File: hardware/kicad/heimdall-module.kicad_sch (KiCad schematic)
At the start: 27 parts, among them J2 Breakout, U1 MC33269DT-3.3G, U2 ESP32-C3-WROOM-02-N4, U3 TYPEC-214-ARP14H105, U4 USBLC6-2SC6

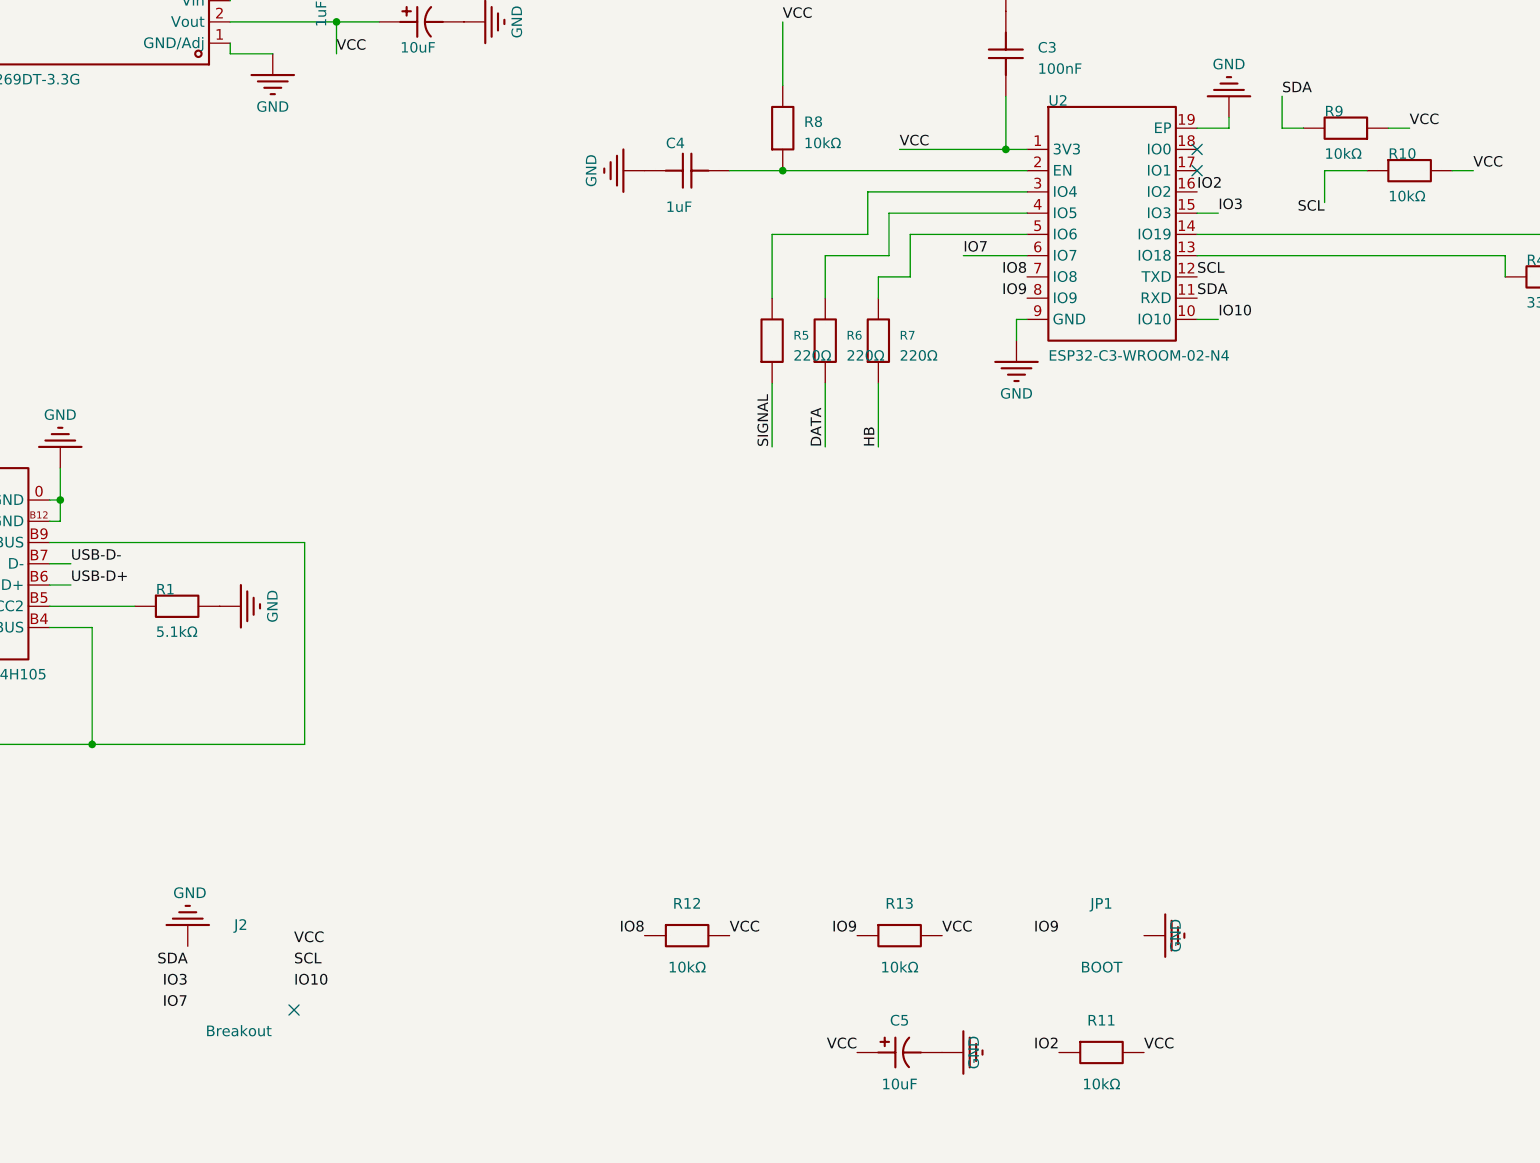
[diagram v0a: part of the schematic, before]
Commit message: Bay interface: Schottky isolation on all bay signal lines
The bay lines no longer connect straight to the ESP32 through 220R
(R5-R7 removed). Each line goes through a BAT54WS (D3-D6), the same
scheme as the DIY Multiprotocol module: the radio can only pull a line
low, and every high level comes from 3V3 pull-ups. A radio driving 5V
can't reach the ESP32.

- PPM in: D3 + R14 4.7k -> IO4
- DATA (CRSF, half duplex): RX D4 + R16 4.7k -> IO5, TX D5 <- IO6,
  R17 1.5k bay-side pull-up for fast rising edges
- HB out: D6 <- IO7, R15 4.7k bay-side pull-up
- Breakout J2 pin 7: IO7 -> IO1 (silk relabelled)

Board re-routed (prep -> Freerouting -> finish pipeline). DRC: 0 errors,
0 unconnected, 0 parity; only the known U3 A1 starved-thermal warning.

Co-Authored-By: Claude Opus 5.5 <noreply@anthropic.com>
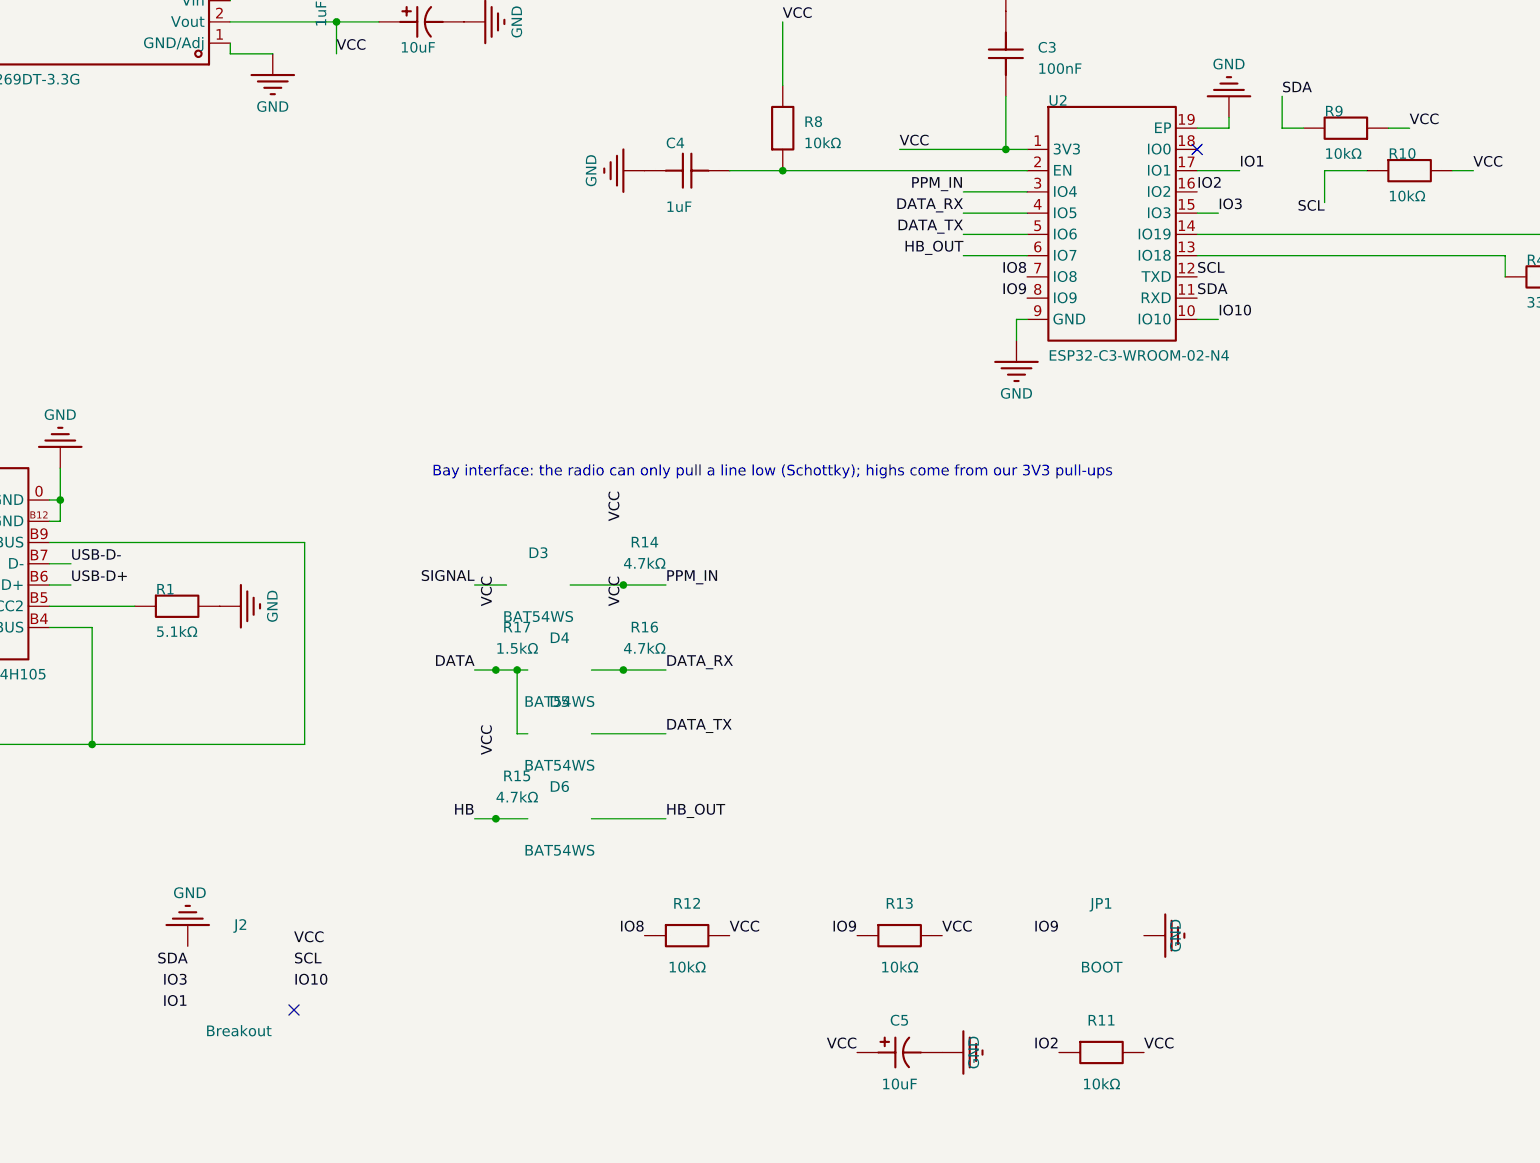
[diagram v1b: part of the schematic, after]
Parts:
- removed R5, R6, R7: 220Ω, heimdall-m-easyedapro:R0805, symbol heimdall-m-easyedapro:ERA6AEB221V
- added D3, D4, D5, D6: BAT54WS, Diode_SMD:D_SOD-323, symbol Device:D_Schottky
- added R14, R15, R16: 4.7kΩ, heimdall-m-easyedapro:R0805, symbol Device:R
- added R17: 1.5kΩ, heimdall-m-easyedapro:R0805, symbol Device:R
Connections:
- net DATA: now also D4.1 (K), D5.2 (A), R17.2
- net HB: now also D6.2 (A), R15.2
- net SIGNAL: now also D3.1 (K)
- net VCC: now also R14.1, R15.1, R16.1, R17.1
- net DATA_TX: now reaches U2.5 (IO6)
- net DATA_TX: now also D5.1 (K)
- net DATA_RX: now reaches U2.4 (IO5)
- net DATA_RX: now also D4.2 (A), R16.2
- net IO1: now reaches U2.17 (IO1)
- net IO1: now also J2.7 (Pin_7)
- net PPM_IN: now reaches U2.3 (IO4)
- net PPM_IN: now also D3.2 (A), R14.2
- net IO7 renamed HB_OUT
- net HB_OUT: now also D6.1 (K); no longer J2.7 (Pin_7)
- no-connect marks 3 -> 2
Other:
- note added: "Bay interface: the radio can only pull a line low (Schottky); highs come from our 3V3 pull-ups"

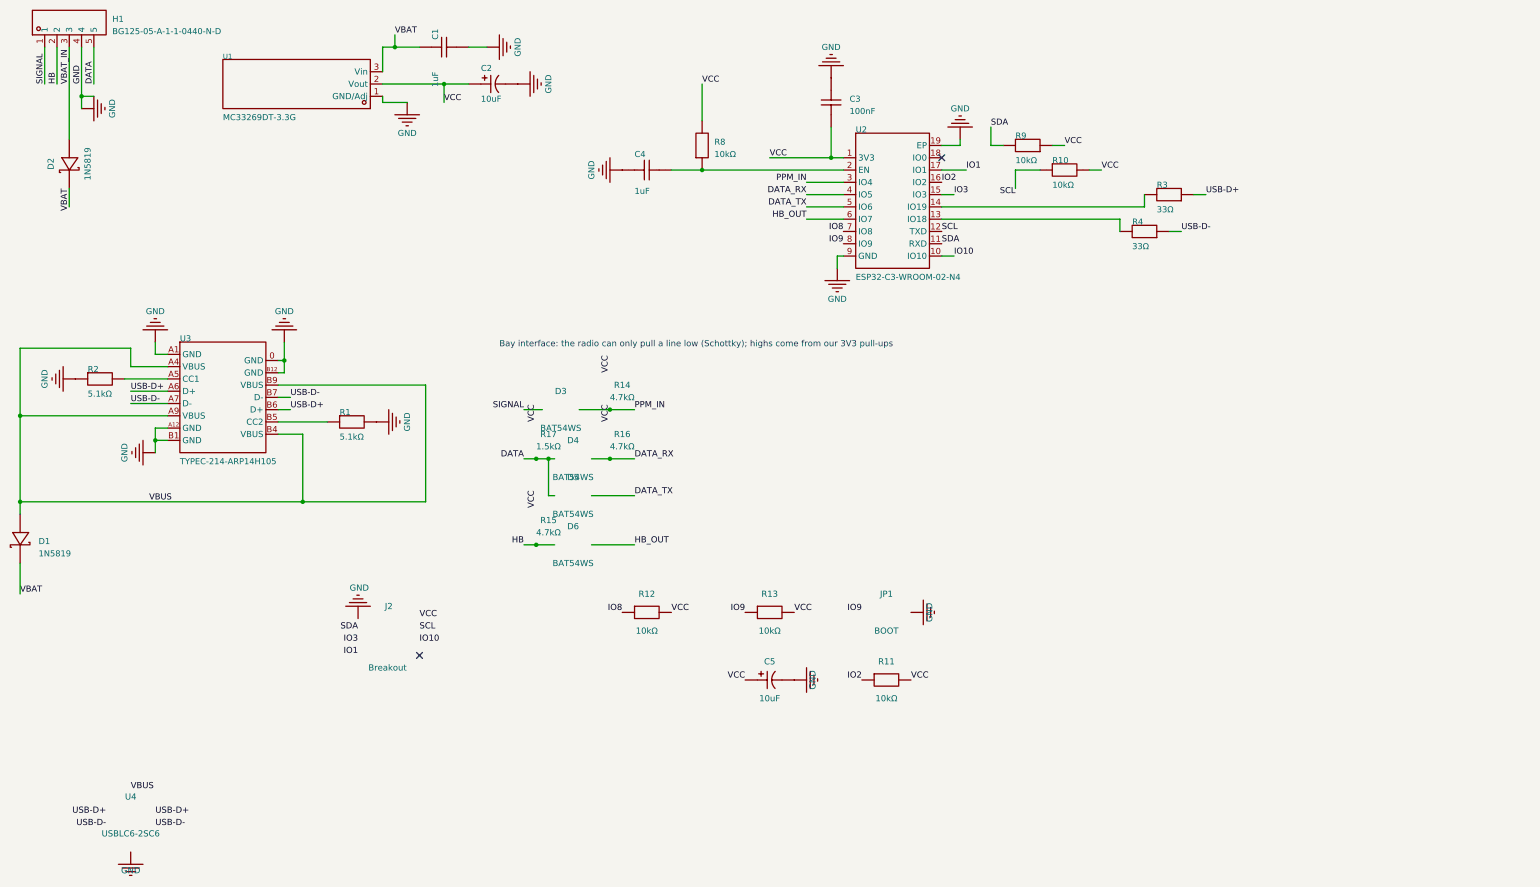
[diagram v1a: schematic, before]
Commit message: Bay DATA transmit through a 5V-tolerant buffer: S.Port and CRSF
The module has to talk S.Port (idle low, inverted) or CRSF (idle high)
on the DATA pin depending on what the internal module uses. The
pull-low-only diode and the 1.5k pull-up only worked for CRSF.

- D5 and the 1.5k pull-up out; U5 74LVC1G34 (always on) + R17 1k in.
  The UART idle level holds the line in either mode; the radio
  overrides 1k when it transmits.
- DATA_TX on IO7, HB_OUT on IO8 (R12 doubles as its pull-up), IO6 free.
- D6/R15 one step lower, R12/R13 0.3mm lower; DATA, HB, HB_OUT, D+/D-
  and the U5 supply hand-routed in route_pcb.py prep.

DRC: 0 unconnected, 0 parity. Two starved-thermal warnings: U3 A1 (as
before) and J2 pin 1 (plated through, connected on the bottom).

Co-Authored-By: Claude Opus 5.5 <noreply@anthropic.com>
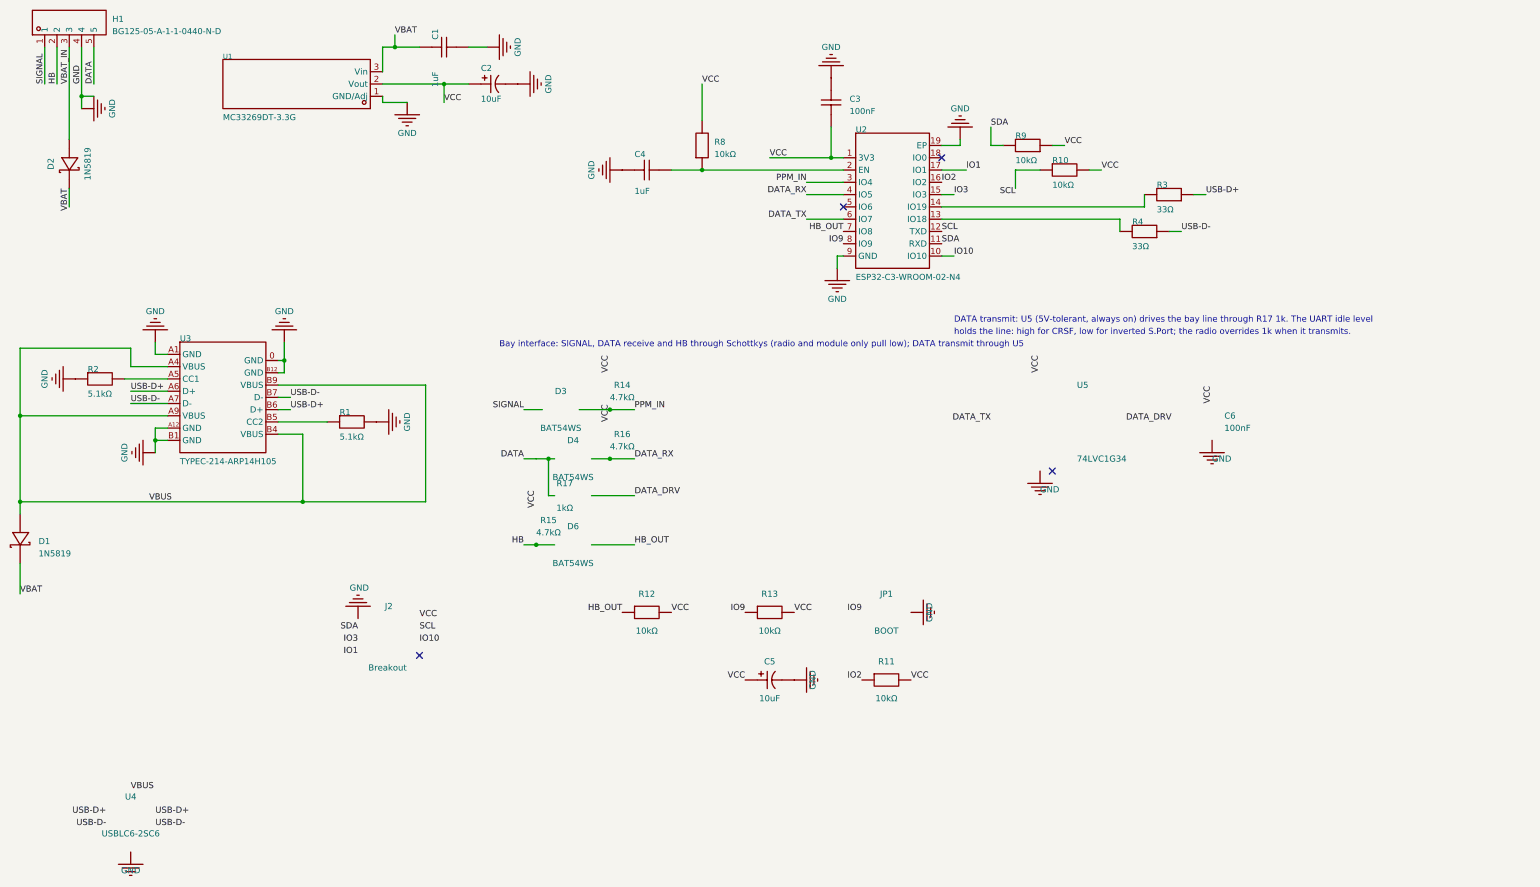
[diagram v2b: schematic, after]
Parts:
- removed D5: BAT54WS, Diode_SMD:D_SOD-323, symbol Device:D_Schottky
- added C6: 100nF, heimdall-m-easyedapro:C0805, symbol Device:C
- added U5: 74LVC1G34, Package_TO_SOT_SMD:SOT-23-5, symbol 74xGxx:74LVC1G34
- R17: value 1.5kΩ -> 1kΩ; Manufacturer Part ERJ-6ENF1501V -> ERJ-6ENF1001V
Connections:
- net IO8 is gone; now on net HB_OUT: R12.1, U2.7 (IO8)
- net DATA: now also R17.1; no longer R17.2
- net DATA_TX: now also U2.6 (IO7), U5.2; no longer U2.5 (IO6)
- net GND: now also C6.2, U5.3 (GND)
- net HB_OUT: no longer U2.6 (IO7)
- net VCC: now also C6.1, U5.5 (VCC); no longer R17.1
- new net DATA_DRV: R17.2, U5.4
- no-connect marks 2 -> 4
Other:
- note added: "Bay interface: SIGNAL, DATA receive and HB through Schottkys (radio and module only pull low); DATA transmit through U5"
- note added: "DATA transmit: U5 (5V-tolerant, always on) drives the bay line through R17 1k. The UART idle level"
- note added: "holds the line: high for CRSF, low for inverted S.Port; the radio overrides 1k when it transmits."
- note removed: "Bay interface: the radio can only pull a line low (Schottky); highs come from our 3V3 pull-ups"

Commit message: Fit the case's lid bosses, M2 screws, spread parts for hand soldering
Case fit (measured on the printed case):
- Board corners chamfered 45 deg (2.8mm legs): the lid screw bosses
  (1.7mm holes, 3.5mm bosses in the cavity corners) stopped the board
  on its way down to the standoffs. ~0.47mm left to each boss.
- MH1-MH3 3.2mm (M3) -> 2.2mm for 2mm self-tapping screws into the
  standoffs' 1.8mm pilots; the lid uses the same screws. Copper keepout
  stays 3mm.

Layout (spread_place.py, then the route_pcb.py flow re-run in full):
- Left of the module: >= 1mm between courtyards, parts in module pin
  order; HB and BOOT parts moved below the module, left of J1.
- U1 at the bottom edge with its heatsink copper; C1/C2 beside it.
- R3/R4 off the module and turned 180, D1 up from D2, R9/R10 apart.
- Hand routes for VCC, HB, SIGNAL, DATA redrawn; 3V3 junction via by
  module pin 1 0.7/0.3 so EN runs straight; U5 GND via.

Silkscreen and numbering:
- All reference designators on top silk, 1.0mm (silk_refs.py).
- Renumbered without gaps: J2->J1, D6->D5, R8..R17->R5..R14
  (bay_pcb.py, rev_pcb.py, case_place.py keep the names of their time).

Export: jlc_export.py (from heimdall-switch) writes the Gerber/drill
package to hardware/kicad/gerber/ (ignored); board plot settings now
Protel extensions, mask subtracted from silk.

ERC 0. DRC 0 unconnected, 0 parity; 2 starved-thermal warnings on U3
A1/A12 as before.

Co-Authored-By: Claude Opus 5.5 <noreply@anthropic.com>
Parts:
- renumbered D6 to D5, J2 to J1, R13 to R10, R14 to R11, R15 to R12, R16 to R13, R17 to R14, R8 to R5, R9 to R6, R10 to R7, R11 to R8, R12 to R9
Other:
- note added: "DATA transmit: U5 (5V-tolerant, always on) drives the bay line through R14 1k. The UART idle level"
- note removed: "DATA transmit: U5 (5V-tolerant, always on) drives the bay line through R17 1k. The UART idle level"
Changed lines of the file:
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@@
 		(in_pos_files yes)
 		(dnp no)
-		(property "Reference" "R12"
+		(property "Reference" "R9"
 			(at 147.32 139.7 0)
 			(show_name no)
@@
 			(project "heimdall-module"
 				(path "/086f1e9c-4772-4202-855e-19c4ce2126c1"
-					(reference "R12")
+					(reference "R9")
 					(unit 1)
 				)
@@
 		(in_pos_files yes)
 		(dnp no)
-		(property "Reference" "R11"
+		(property "Reference" "R8"
 			(at 196.85 153.67 0)
 			(show_name no)
@@
 			(project "heimdall-module"
 				(path "/086f1e9c-4772-4202-855e-19c4ce2126c1"
-					(reference "R11")
+					(reference "R8")
 					(unit 1)
 				)
@@
 		(in_pos_files yes)
 		(dnp no)
-		(property "Reference" "R10"
+		(property "Reference" "R7"
 			(at 231.14 50.8 0)
 			(show_name no)
@@
 			(project "heimdall-module"
 				(path "/086f1e9c-4772-4202-855e-19c4ce2126c1"
-					(reference "R10")
+					(reference "R7")
 					(unit 1)
 				)
@@
 		(in_pos_files yes)
 		(dnp no)
-		(property "Reference" "J2"
+		(property "Reference" "J1"
 			(at 93.98 142.24 0)
 			(show_name no)
@@
 			(project "heimdall-module"
 				(path "/086f1e9c-4772-4202-855e-19c4ce2126c1"
-					(reference "J2")
+					(reference "J1")
 					(unit 1)
 				)
@@
 		(in_pos_files yes)
 		(dnp no)
-		(property "Reference" "R9"
+		(property "Reference" "R6"
 			(at 223.52 45.72 0)
 			(show_name no)
@@
 			(project "heimdall-module"
 				(path "/086f1e9c-4772-4202-855e-19c4ce2126c1"
-					(reference "R9")
+					(reference "R6")
 					(unit 1)
 				)
@@
 		(in_pos_files yes)
 		(dnp no)
-		(property "Reference" "R8"
+		(property "Reference" "R5"
 			(at 161.29 46.99 90)
 			(show_name no)
@@
 			(project "heimdall-module"
 				(path "/086f1e9c-4772-4202-855e-19c4ce2126c1"
-					(reference "R8")
+					(reference "R5")
 					(unit 1)
 				)
@@
 		(in_pos_files yes)
 		(dnp no)
-		(property "Reference" "R13"
+		(property "Reference" "R10"
 			(at 172.72 139.7 0)
 			(show_name no)
@@
 			(project "heimdall-module"
 				(path "/086f1e9c-4772-4202-855e-19c4ce2126c1"
-					(reference "R13")
+					(reference "R10")
 					(unit 1)
 				)
@@
 		(in_pos_files yes)
 		(dnp no)
-		(property "Reference" "R14"
+		(property "Reference" "R11"
 			(at 142.24 96.52 0)
 			(show_name no)
@@
 			(project "heimdall-module"
 				(path "/086f1e9c-4772-4202-855e-19c4ce2126c1"
-					(reference "R14")
+					(reference "R11")
 					(unit 1)
 				)
@@
 		(in_pos_files yes)
 		(dnp no)
-		(property "Reference" "R16"
+		(property "Reference" "R13"
 			(at 142.24 106.68 0)
 			(show_name no)
@@
 			(project "heimdall-module"
 				(path "/086f1e9c-4772-4202-855e-19c4ce2126c1"
-					(reference "R16")
+					(reference "R13")
 					(unit 1)
 				)
@@
 		(in_pos_files yes)
 		(dnp no)
-		(property "Reference" "D6"
+		(property "Reference" "D5"
 			(at 132.08 125.73 0)
 			(show_name no)
@@
 			(project "heimdall-module"
 				(path "/086f1e9c-4772-4202-855e-19c4ce2126c1"
-					(reference "D6")
+					(reference "D5")
 					(unit 1)
 				)
@@
 		(in_pos_files yes)
 		(dnp no)
-		(property "Reference" "R15"
+		(property "Reference" "R12"
 			(at 127 124.46 0)
 			(show_name no)
@@
 			(project "heimdall-module"
 				(path "/086f1e9c-4772-4202-855e-19c4ce2126c1"
-					(reference "R15")
+					(reference "R12")
 					(unit 1)
 				)
@@
 		(in_pos_files yes)
 		(dnp no)
-		(property "Reference" "R17"
+		(property "Reference" "R14"
 			(at 132.08 116.84 90)
 			(show_name no)
@@
 			(project "heimdall-module"
 				(path "/086f1e9c-4772-4202-855e-19c4ce2126c1"
-					(reference "R17")
+					(reference "R14")
 					(unit 1)
 				)
@@
 		)
 	)
-	(text "DATA transmit: U5 (5V-tolerant, always on) drives the bay line through R17 1k. The UART idle level"
+	(text "DATA transmit: U5 (5V-tolerant, always on) drives the bay line through R14 1k. The UART idle level"
 		(exclude_from_sim no)
 		(at 210.82 83.82 0)
